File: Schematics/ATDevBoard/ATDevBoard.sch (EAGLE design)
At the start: 39 parts, among them U1 TINY85-DIP

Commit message: Rerun cam on brd file to upload to SeeedStudio, deleted PNG folder
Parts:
- removed C9: 100n, rcl:C-EU050-024X044
- added C5: 100n, SmartPrj:C-EU050-024X044
- C6: value 100n -> 22p
- C7: value 22p -> 100n; device SmartPrj:C-EU050-024X044 -> rcl:C-EU050-024X044
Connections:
- net GND: now also C5.1, C6.2, C7.1; no longer C6.1, C7.2, C9.1
- net VCC: now also C5.2, C8.2; no longer C6.2, C9.2
- net VIN: now also C7.2; no longer C8.2
- net XTAL1: now also C6.1; no longer C7.1
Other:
- moved on the sheet: C6, C7, C8
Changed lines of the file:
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@@
 <part name="GND13" library="supply2" deviceset="GND" device=""/>
 <part name="R7" library="rcl" deviceset="R-US_" device="0207/10" value="1M"/>
-<part name="C6" library="SmartPrj" deviceset="C-EU" device="050-024X044" value="100n"/>
+<part name="C5" library="SmartPrj" deviceset="C-EU" device="050-024X044" value="100n"/>
 <part name="POWER" library="pinhead" deviceset="PINHD-1X5" device="" value="6x1F-H8.5"/>
 <part name="P+4" library="supply1" deviceset="VCC" device=""/>
 <part name="SUPPLY52" library="supply2" deviceset="GND" device=""/>
+<part name="C7" library="rcl" deviceset="C-EU" device="050-024X044" value="100n"/>
 <part name="C8" library="rcl" deviceset="C-EU" device="050-024X044" value="100n"/>
-<part name="C9" library="rcl" deviceset="C-EU" device="050-024X044" value="100n"/>
 <part name="SUPPLY54" library="supply2" deviceset="GND" device=""/>
 <part name="SUPPLY55" library="supply1" deviceset="VCC" device=""/>
@@
 <part name="OSC1" library="special" deviceset="XTAL/S" device=""/>
 <part name="C3" library="SmartPrj" deviceset="C-EU" device="050-024X044" value="22p"/>
-<part name="C7" library="SmartPrj" deviceset="C-EU" device="050-024X044" value="22p"/>
+<part name="C6" library="SmartPrj" deviceset="C-EU" device="050-024X044" value="22p"/>
 <part name="GND3" library="supply2" deviceset="GND" device=""/>
 <part name="R2" library="rcl" deviceset="R-US_" device="0309/12" value="10K"/>
@@
 <attribute name="VALUE" x="55.245" y="118.872" size="1.778" layer="96" rot="MR180"/>
 </instance>
-<instance part="C6" gate="G$1" x="53.34" y="91.44" smashed="yes" rot="R180">
+<instance part="C5" gate="G$1" x="53.34" y="91.44" smashed="yes" rot="R180">
 <attribute name="NAME" x="47.117" y="93.345" size="1.778" layer="95"/>
 <attribute name="VALUE" x="45.466" y="90.805" size="1.778" layer="96"/>
@@
 </instance>
 <instance part="SUPPLY52" gate="GND" x="231.14" y="142.24"/>
-<instance part="C8" gate="G$1" x="231.14" y="152.4" smashed="yes" rot="R180">
+<instance part="C7" gate="G$1" x="231.14" y="152.4" smashed="yes" rot="R180">
 <attribute name="NAME" x="229.616" y="157.099" size="1.778" layer="95" rot="R180"/>
 <attribute name="VALUE" x="229.616" y="152.019" size="1.778" layer="96" rot="R180"/>
 </instance>
-<instance part="C9" gate="G$1" x="274.32" y="152.4" rot="R180"/>
+<instance part="C8" gate="G$1" x="274.32" y="152.4" rot="R180"/>
 <instance part="SUPPLY54" gate="GND" x="274.32" y="144.78"/>
 <instance part="SUPPLY55" gate="VCC" x="274.32" y="165.1" smashed="yes">
@@
 <attribute name="VALUE" x="34.925" y="129.794" size="1.778" layer="96" rot="R270"/>
 </instance>
-<instance part="C7" gate="G$1" x="38.1" y="111.76" smashed="yes" rot="R270">
+<instance part="C6" gate="G$1" x="38.1" y="111.76" smashed="yes" rot="R270">
 <attribute name="NAME" x="36.195" y="105.537" size="1.778" layer="95" rot="R90"/>
 <attribute name="VALUE" x="38.735" y="103.886" size="1.778" layer="96" rot="R90"/>
@@
 </segment>
 <segment>
-<pinref part="C9" gate="G$1" pin="1"/>
+<pinref part="C8" gate="G$1" pin="1"/>
 <pinref part="SUPPLY54" gate="GND" pin="GND"/>
 <wire x1="274.32" y1="147.32" x2="274.32" y2="149.86" width="0.1524" layer="91"/>
@@
 <pinref part="SUPPLY52" gate="GND" pin="GND"/>
 <wire x1="231.14" y1="147.32" x2="231.14" y2="144.78" width="0.1524" layer="91"/>
-<pinref part="C8" gate="G$1" pin="1"/>
+<pinref part="C7" gate="G$1" pin="1"/>
 <wire x1="231.14" y1="149.86" x2="231.14" y2="147.32" width="0.1524" layer="91"/>
 <junction x="231.14" y="147.32"/>
@@
 </segment>
 <segment>
-<pinref part="C6" gate="G$1" pin="1"/>
+<pinref part="C5" gate="G$1" pin="1"/>
 <wire x1="53.34" y1="88.9" x2="53.34" y2="86.36" width="0.1524" layer="91"/>
 <pinref part="GND2" gate="GND" pin="GND"/>
@@
 <wire x1="33.02" y1="121.92" x2="30.48" y2="121.92" width="0.1524" layer="91"/>
 <wire x1="30.48" y1="121.92" x2="30.48" y2="111.76" width="0.1524" layer="91"/>
-<pinref part="C7" gate="G$1" pin="2"/>
+<pinref part="C6" gate="G$1" pin="2"/>
 <wire x1="30.48" y1="111.76" x2="33.02" y2="111.76" width="0.1524" layer="91"/>
 <pinref part="GND3" gate="GND" pin="GND"/>
@@
 <net name="VIN" class="1">
 <segment>
-<pinref part="C8" gate="G$1" pin="2"/>
+<pinref part="C7" gate="G$1" pin="2"/>
 <pinref part="D3" gate="1" pin="C"/>
 <wire x1="241.3" y1="167.64" x2="231.14" y2="167.64" width="0.1524" layer="91"/>
@@
 <pinref part="R7" gate="G$1" pin="1"/>
 <pinref part="OSC1" gate="G$1" pin="1"/>
-<pinref part="C7" gate="G$1" pin="1"/>
+<pinref part="C6" gate="G$1" pin="1"/>
 <wire x1="40.64" y1="111.76" x2="45.72" y2="111.76" width="0.1524" layer="91"/>
 <junction x="45.72" y="111.76"/>
@@
 <pinref part="P+3" gate="VCC" pin="VCC"/>
 <pinref part="ZU4" gate="G$1" pin="AVCC"/>
-<pinref part="C6" gate="G$1" pin="2"/>
+<pinref part="C5" gate="G$1" pin="2"/>
 </segment>
 <segment>
@@
 </segment>
 <segment>
-<pinref part="C9" gate="G$1" pin="2"/>
+<pinref part="C8" gate="G$1" pin="2"/>
 <pinref part="SUPPLY55" gate="VCC" pin="VCC"/>
 <wire x1="274.32" y1="162.56" x2="274.32" y2="160.02" width="0.1524" layer="91"/>

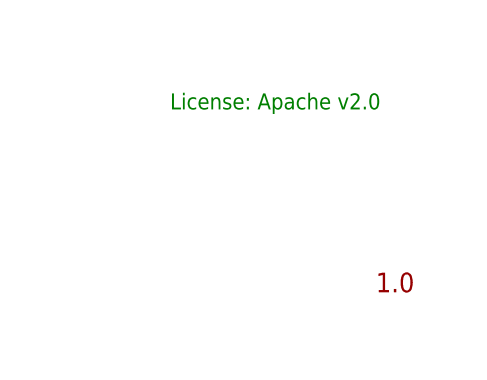
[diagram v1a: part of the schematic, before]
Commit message: Fixed 1M resistor package, and header distance in PCB
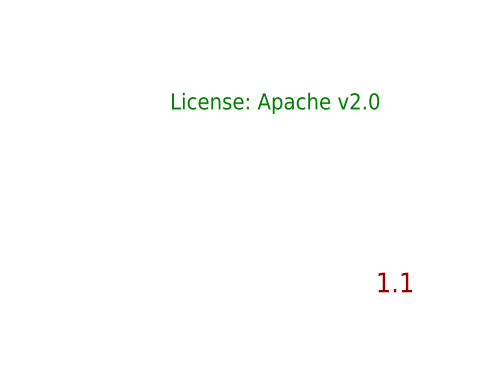
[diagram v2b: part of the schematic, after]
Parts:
- R7: device rcl:R-US_0207/10 -> rcl:R-US_0309/12
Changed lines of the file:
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@@
 <grid distance="0.1" unitdist="inch" unit="inch" style="lines" multiple="1" display="no" altdistance="0.01" altunitdist="inch" altunit="inch"/>
 <layers>
-<layer number="1" name="Top" color="4" fill="1" visible="no" active="no"/>
-<layer number="16" name="Bottom" color="1" fill="1" visible="no" active="no"/>
-<layer number="17" name="Pads" color="2" fill="1" visible="no" active="no"/>
-<layer number="18" name="Vias" color="2" fill="1" visible="no" active="no"/>
-<layer number="19" name="Unrouted" color="6" fill="1" visible="no" active="no"/>
-<layer number="20" name="Dimension" color="15" fill="1" visible="no" active="no"/>
-<layer number="21" name="tPlace" color="7" fill="1" visible="no" active="no"/>
-<layer number="22" name="bPlace" color="7" fill="1" visible="no" active="no"/>
-<layer number="23" name="tOrigins" color="15" fill="1" visible="no" active="no"/>
-<layer number="24" name="bOrigins" color="15" fill="1" visible="no" active="no"/>
-<layer number="25" name="tNames" color="7" fill="1" visible="no" active="no"/>
-<layer number="26" name="bNames" color="7" fill="1" visible="no" active="no"/>
-<layer number="27" name="tValues" color="7" fill="1" visible="no" active="no"/>
-<layer number="28" name="bValues" color="7" fill="1" visible="no" active="no"/>
+<layer number="1" name="Top" color="4" fill="1" visible="yes" active="no"/>
+<layer number="16" name="Bottom" color="1" fill="1" visible="yes" active="no"/>
+<layer number="17" name="Pads" color="2" fill="1" visible="yes" active="no"/>
+<layer number="18" name="Vias" color="2" fill="1" visible="yes" active="no"/>
+<layer number="19" name="Unrouted" color="6" fill="1" visible="yes" active="no"/>
+<layer number="20" name="Dimension" color="15" fill="1" visible="yes" active="no"/>
+<layer number="21" name="tPlace" color="7" fill="1" visible="yes" active="no"/>
+<layer number="22" name="bPlace" color="7" fill="1" visible="yes" active="no"/>
+<layer number="23" name="tOrigins" color="15" fill="1" visible="yes" active="no"/>
+<layer number="24" name="bOrigins" color="15" fill="1" visible="yes" active="no"/>
+<layer number="25" name="tNames" color="7" fill="1" visible="yes" active="no"/>
+<layer number="26" name="bNames" color="7" fill="1" visible="yes" active="no"/>
+<layer number="27" name="tValues" color="7" fill="1" visible="yes" active="no"/>
+<layer number="28" name="bValues" color="7" fill="1" visible="yes" active="no"/>
 <layer number="29" name="tStop" color="7" fill="3" visible="no" active="no"/>
 <layer number="30" name="bStop" color="7" fill="6" visible="no" active="no"/>
@@
 <layer number="35" name="tGlue" color="7" fill="4" visible="no" active="no"/>
 <layer number="36" name="bGlue" color="7" fill="5" visible="no" active="no"/>
-<layer number="37" name="tTest" color="7" fill="1" visible="no" active="no"/>
-<layer number="38" name="bTest" color="7" fill="1" visible="no" active="no"/>
+<layer number="37" name="tTest" color="7" fill="1" visible="yes" active="no"/>
+<layer number="38" name="bTest" color="7" fill="1" visible="yes" active="no"/>
 <layer number="39" name="tKeepout" color="4" fill="11" visible="no" active="no"/>
 <layer number="40" name="bKeepout" color="1" fill="11" visible="no" active="no"/>
@@
 <layer number="44" name="Drills" color="7" fill="1" visible="no" active="no"/>
 <layer number="45" name="Holes" color="7" fill="1" visible="no" active="no"/>
-<layer number="46" name="Milling" color="3" fill="1" visible="no" active="no"/>
-<layer number="47" name="Measures" color="7" fill="1" visible="no" active="no"/>
-<layer number="48" name="Document" color="7" fill="1" visible="no" active="no"/>
-<layer number="49" name="Reference" color="7" fill="1" visible="no" active="no"/>
-<layer number="50" name="dxf" color="12" fill="1" visible="no" active="no"/>
-<layer number="51" name="tDocu" color="7" fill="1" visible="no" active="no"/>
-<layer number="52" name="bDocu" color="7" fill="1" visible="no" active="no"/>
-<layer number="53" name="tGND_GNDA" color="7" fill="1" visible="no" active="no"/>
-<layer number="54" name="bGND_GNDA" color="7" fill="1" visible="no" active="no"/>
-<layer number="56" name="wert" color="7" fill="1" visible="no" active="no"/>
-<layer number="57" name="tCAD" color="7" fill="1" visible="no" active="no"/>
-<layer number="59" name="tCarbon" color="7" fill="1" visible="no" active="no"/>
-<layer number="60" name="bCarbon" color="7" fill="1" visible="no" active="no"/>
+<layer number="46" name="Milling" color="3" fill="1" visible="yes" active="no"/>
+<layer number="47" name="Measures" color="7" fill="1" visible="yes" active="no"/>
+<layer number="48" name="Document" color="7" fill="1" visible="yes" active="no"/>
+<layer number="49" name="Reference" color="7" fill="1" visible="yes" active="no"/>
+<layer number="50" name="dxf" color="12" fill="1" visible="yes" active="no"/>
+<layer number="51" name="tDocu" color="7" fill="1" visible="yes" active="no"/>
+<layer number="52" name="bDocu" color="7" fill="1" visible="yes" active="no"/>
+<layer number="53" name="tGND_GNDA" color="7" fill="1" visible="yes" active="no"/>
+<layer number="54" name="bGND_GNDA" color="7" fill="1" visible="yes" active="no"/>
+<layer number="56" name="wert" color="7" fill="1" visible="yes" active="no"/>
+<layer number="57" name="tCAD" color="7" fill="1" visible="yes" active="no"/>
+<layer number="59" name="tCarbon" color="7" fill="1" visible="yes" active="no"/>
+<layer number="60" name="bCarbon" color="7" fill="1" visible="yes" active="no"/>
 <layer number="90" name="Modules" color="5" fill="1" visible="yes" active="yes"/>
 <layer number="91" name="Nets" color="2" fill="1" visible="yes" active="yes"/>
@@
 <schematic xreflabel="%F%N/%S" xrefpart="/%S.%C%R">
 <attributes>
-<attribute name="VERSION" value="1.0"/>
+<attribute name="VERSION" value="1.1"/>
 </attributes>
 <variantdefs>
@@
 <part name="C4" library="SmartPrj" deviceset="C-EU" device="050-024X044" value="100n"/>
 <part name="GND13" library="supply2" deviceset="GND" device=""/>
-<part name="R7" library="rcl" deviceset="R-US_" device="0207/10" value="1M"/>
+<part name="R7" library="rcl" deviceset="R-US_" device="0309/12" value="1M"/>
 <part name="C5" library="SmartPrj" deviceset="C-EU" device="050-024X044" value="100n"/>
 <part name="POWER" library="pinhead" deviceset="PINHD-1X5" device="" value="6x1F-H8.5"/>
